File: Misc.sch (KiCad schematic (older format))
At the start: 22 parts, among them U3 PCF8523TK, U4 TLV70218DBV, U5 CDCE913PW, U7 LM75BDP, U8 LM75BDP, X1 32768, X2 20MHz

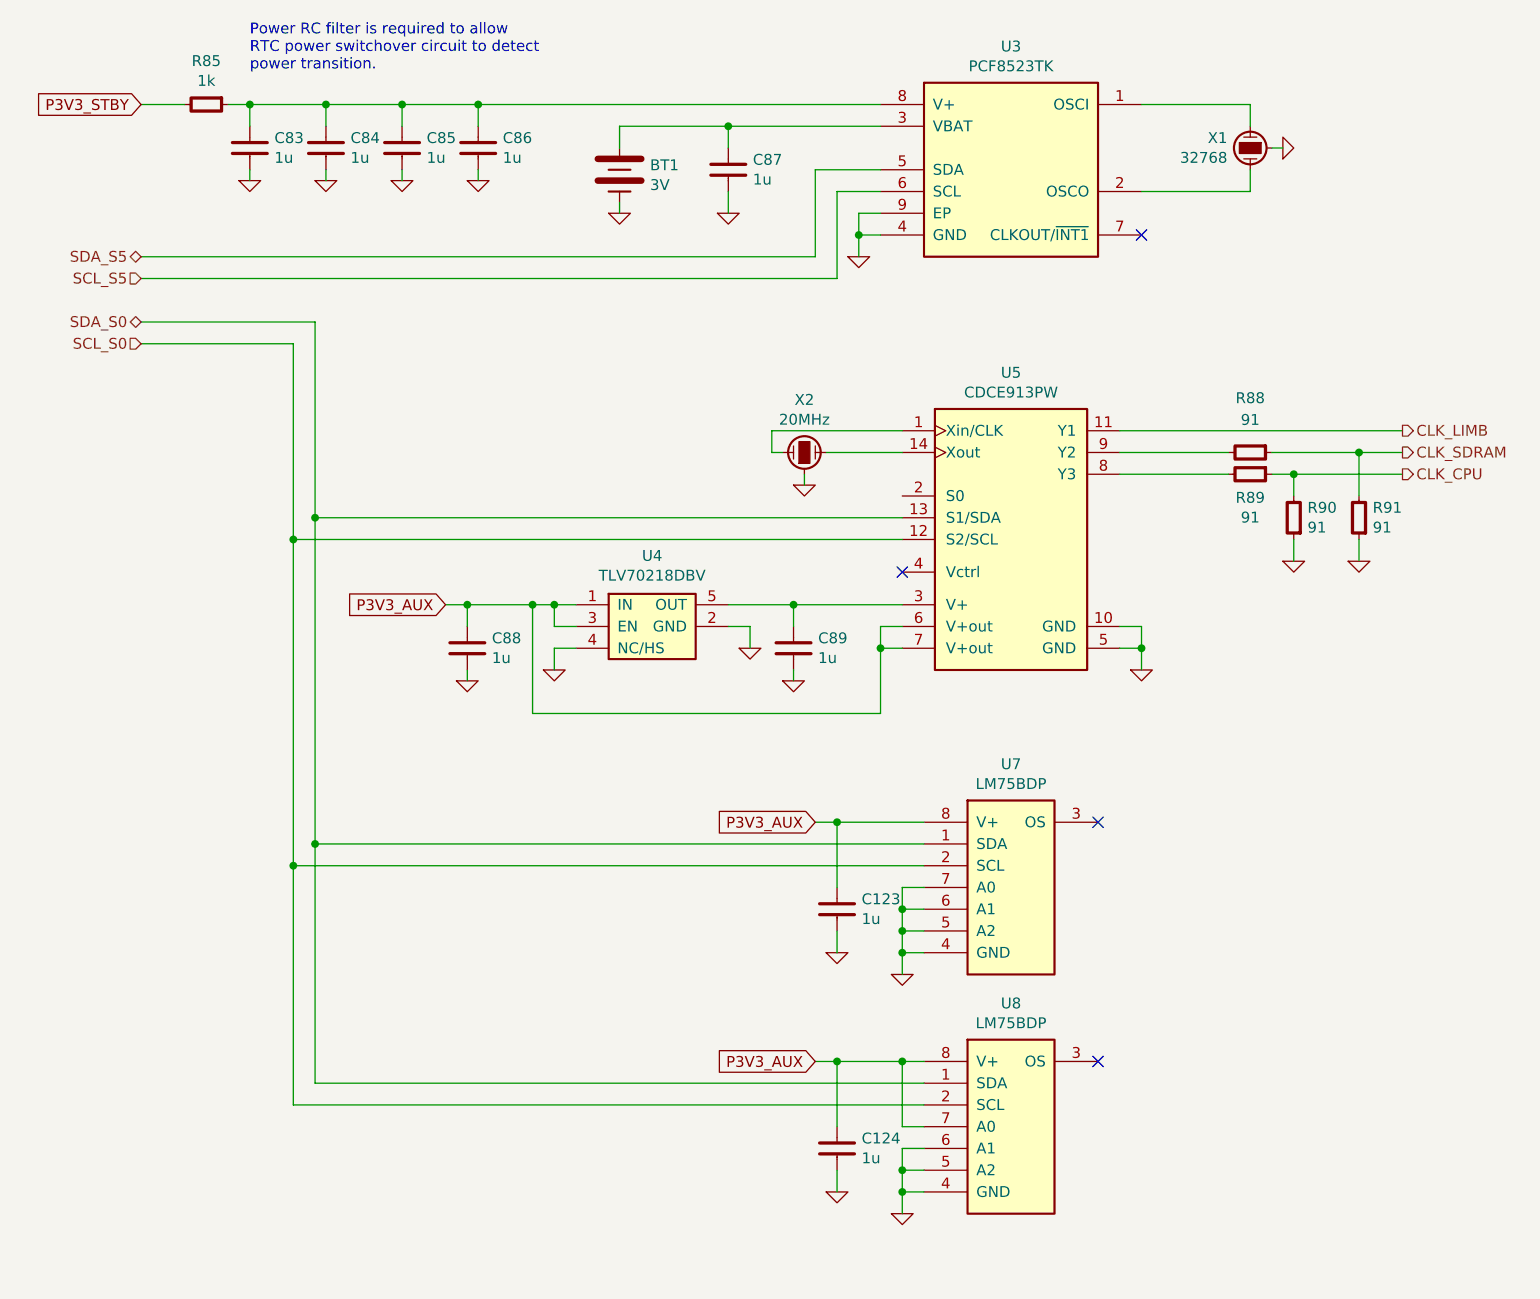
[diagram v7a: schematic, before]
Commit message: Tidy up Misc sheet
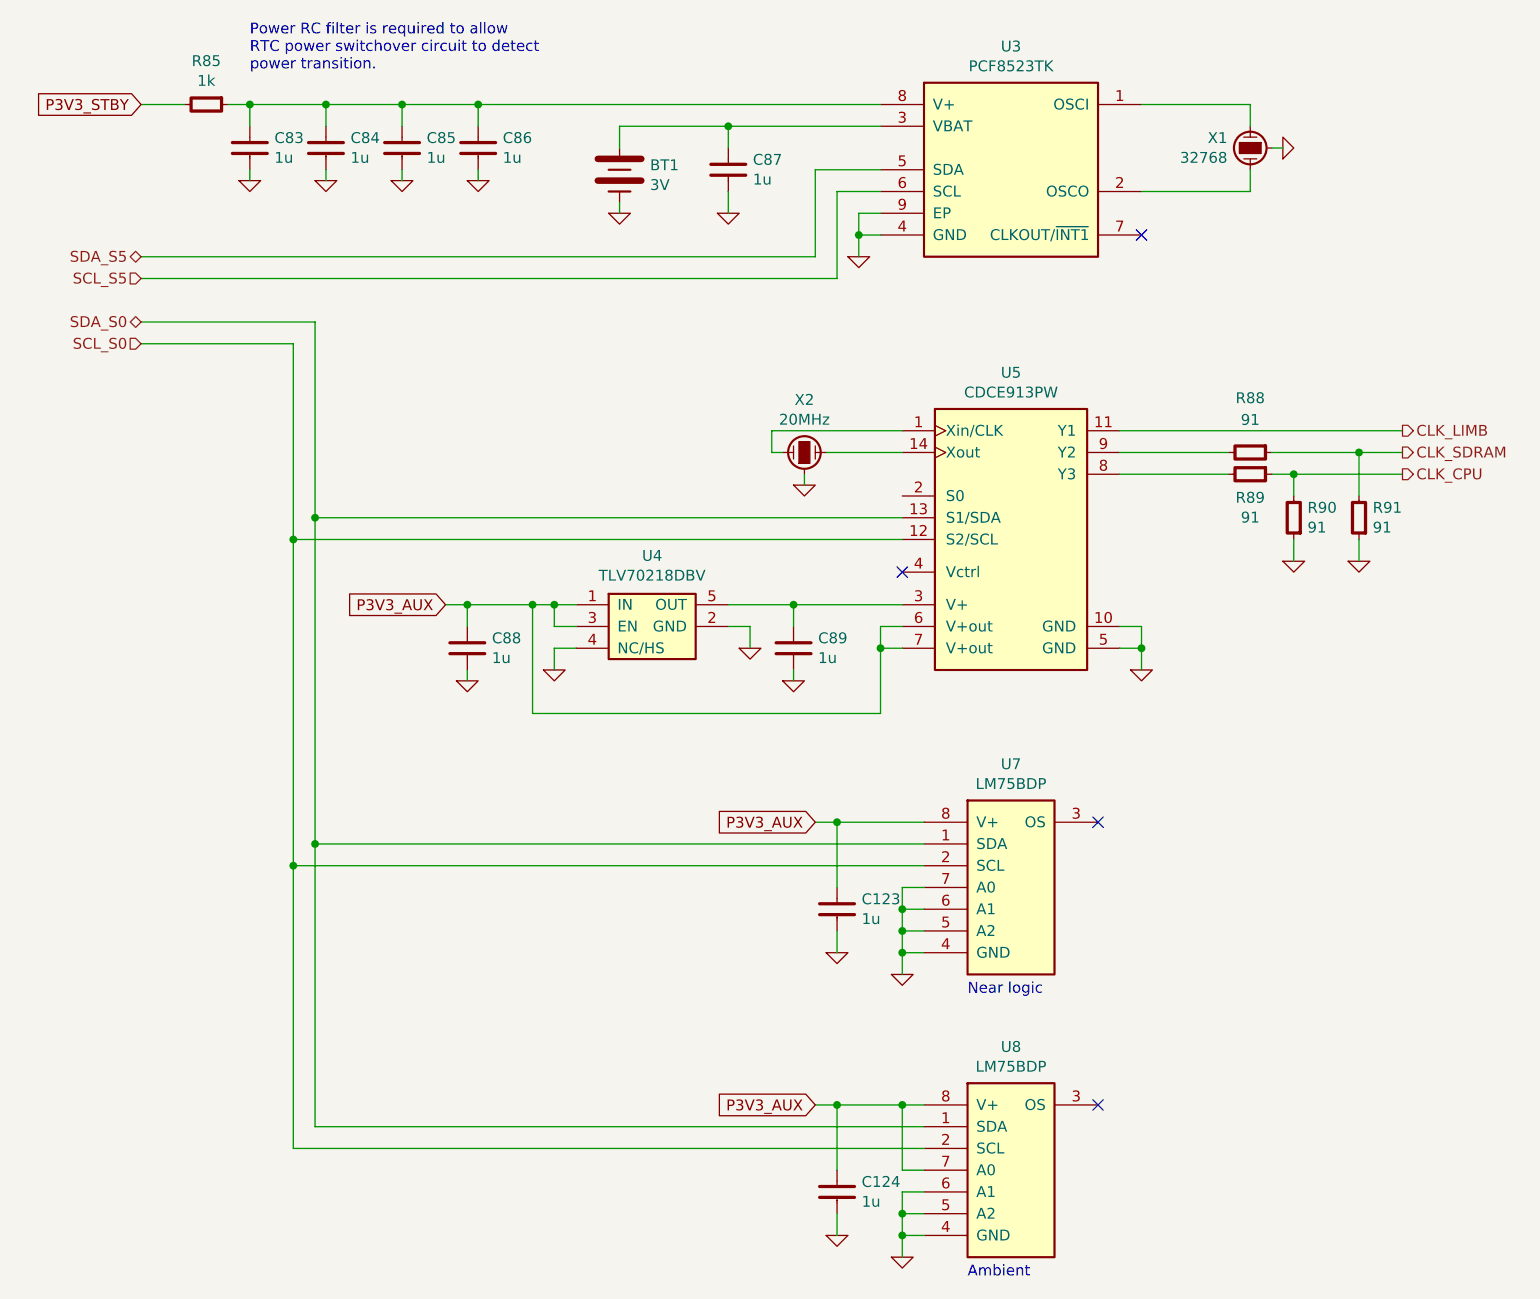
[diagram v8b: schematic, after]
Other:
- note added: "Ambient"
- note added: "Near logic"
- moved on the sheet: C124, U8
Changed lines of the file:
@@
 EELAYER 25 0
 EELAYER END
-$Descr A4 11693 8268
+$Descr A 11000 8500
 encoding utf-8
-Sheet 9 10
-Title ""
-Date ""
+Sheet 8 10
+Title "Miscellaneous peripherals"
+Date "2016-08-05"
 Rev ""
 Comp ""
@@
 	5000 2000 4900 2000
 Wire Wire Line
-	4900 2000 4900 2200
+	4900 2000 4900 2100
+Wire Wire Line
+	4900 2100 4900 2200
 Wire Wire Line
 	5000 2100 4900 2100
@@
 $EndComp
 Wire Wire Line
-	2000 1500 5000 1500
+	2000 1500 2100 1500
+Wire Wire Line
+	2100 1500 2450 1500
+Wire Wire Line
+	2450 1500 2800 1500
+Wire Wire Line
+	2800 1500 3150 1500
+Wire Wire Line
+	3150 1500 5000 1500
 $Comp
 L C-0402 C?
@@
 $EndComp
 Wire Wire Line
-	3800 1600 5000 1600
+	3800 1600 4300 1600
+Wire Wire Line
+	4300 1600 5000 1600
 Wire Wire Line
 	3800 1600 3800 1700
@@
 	6100 3900 6200 3900
 Wire Wire Line
-	6200 3900 6200 4100
+	6200 3900 6200 4000
+Wire Wire Line
+	6200 4000 6200 4100
 Wire Wire Line
 	6200 4000 6100 4000
@@
 $EndComp
 Wire Wire Line
-	4300 3800 5100 3800
+	4300 3800 4600 3800
+Wire Wire Line
+	4600 3800 5100 3800
 $Comp
 L GND #PWR161
@@
 	3500 3900 3500 3800
 Wire Wire Line
-	3000 3800 3600 3800
+	3000 3800 3100 3800
+Wire Wire Line
+	3100 3800 3400 3800
+Wire Wire Line
+	3400 3800 3500 3800
+Wire Wire Line
+	3500 3800 3600 3800
 Connection ~ 3500 3800
 Text GLabel 3000 3800 0    50   Input ~ 0
@@
 	4600 4150 4600 4100
 Wire Wire Line
-	5000 4300 5000 3900
+	5000 4300 5000 4000
+Wire Wire Line
+	5000 4000 5000 3900
 $Comp
 L LM75BDP U7
@@
 P3V3_AUX
 Wire Wire Line
-	4700 4800 5200 4800
+	4700 4800 4800 4800
+Wire Wire Line
+	4800 4800 5200 4800
 Text HLabel 1600 2500 0    50   BiDi ~ 0
 SDA_S0
@@
 	1600 2500 2400 2500
 Wire Wire Line
-	2400 2500 2400 6000
-Wire Wire Line
-	2300 2600 2300 6100
+	2400 2500 2400 3400
+Wire Wire Line
+	2400 3400 2400 4900
+Wire Wire Line
+	2400 4900 2400 6200
+Wire Wire Line
+	2300 2600 2300 3500
+Wire Wire Line
+	2300 3500 2300 5000
+Wire Wire Line
+	2300 5000 2300 6300
 Wire Wire Line
 	2300 2600 1600 2600
@@
 $EndComp
 Wire Wire Line
-	5100 5100 5100 5500
+	5100 5100 5100 5200
+Wire Wire Line
+	5100 5200 5100 5300
+Wire Wire Line
+	5100 5300 5100 5400
+Wire Wire Line
+	5100 5400 5100 5500
 Wire Wire Line
 	5100 5100 5200 5100
@@
 L LM75BDP U8
 U 1 1 579F50E6
-P 5600 5900
-F 0 "U8" H 5600 6167 50  0000 C CNN
-F 1 "LM75BDP" H 5600 6076 50  0000 C CNN
-F 2 "IPC7351-Nominal:SOP65P490X110-8" H 5600 5100 50  0001 C CNN
-F 3 "http://www.nxp.com/documents/data_sheet/LM75B.pdf" H 5600 4900 50  0001 C CNN
-F 4 "IC NXP LM75BDP" H 5600 5000 50  0001 C CNN "BOM"
-	1    5600 5900
-	1    0    0    -1
-$EndComp
-NoConn ~ 6000 5900
-Text GLabel 4700 5900 0    50   Input ~ 0
+P 5600 6100
+F 0 "U8" H 5600 6367 50  0000 C CNN
+F 1 "LM75BDP" H 5600 6276 50  0000 C CNN
+F 2 "IPC7351-Nominal:SOP65P490X110-8" H 5600 5300 50  0001 C CNN
+F 3 "http://www.nxp.com/documents/data_sheet/LM75B.pdf" H 5600 5100 50  0001 C CNN
+F 4 "IC NXP LM75BDP" H 5600 5200 50  0001 C CNN "BOM"
+	1    5600 6100
+	1    0    0    -1
+$EndComp
+NoConn ~ 6000 6100
+Text GLabel 4700 6100 0    50   Input ~ 0
 P3V3_AUX
 Wire Wire Line
-	4700 5900 5200 5900
-Wire Wire Line
-	2400 6000 5200 6000
+	4700 6100 4800 6100
+Wire Wire Line
+	4800 6100 5100 6100
+Wire Wire Line
+	5100 6100 5200 6100
+Wire Wire Line
+	2400 6200 5200 6200
 Connection ~ 2400 4900
 Wire Wire Line
-	2300 6100 5200 6100
+	2300 6300 5200 6300
 Connection ~ 2300 5000
 Wire Wire Line
-	5200 6300 5100 6300
-Wire Wire Line
-	5100 6300 5100 6600
+	5200 6500 5100 6500
+Wire Wire Line
+	5100 6500 5100 6600
+Wire Wire Line
+	5100 6600 5100 6700
+Wire Wire Line
+	5100 6700 5100 6800
 $Comp
 L GND #PWR168
 U 1 1 579F532E
-P 5100 6600
-F 0 "#PWR168" H 5100 6600 30  0001 C CNN
-F 1 "GND" H 5100 6530 30  0001 C CNN
-F 2 "" H 5100 6600 60  0000 C CNN
-F 3 "" H 5100 6600 60  0000 C CNN
-	1    5100 6600
-	1    0    0    -1
-$EndComp
+P 5100 6800
+F 0 "#PWR168" H 5100 6800 30  0001 C CNN
+F 1 "GND" H 5100 6730 30  0001 C CNN
+F 2 "" H 5100 6800 60  0000 C CNN
+F 3 "" H 5100 6800 60  0000 C CNN
+	1    5100 6800
+	1    0    0    -1
+$EndComp
+Wire Wire Line
+	5200 6600 5100 6600
+Connection ~ 5100 6600
+Wire Wire Line
+	5200 6700 5100 6700
+Connection ~ 5100 6700
 Wire Wire Line
 	5200 6400 5100 6400
-Connection ~ 5100 6400
-Wire Wire Line
-	5200 6500 5100 6500
-Connection ~ 5100 6500
-Wire Wire Line
-	5200 6200 5100 6200
-Wire Wire Line
-	5100 6200 5100 5900
-Connection ~ 5100 5900
+Wire Wire Line
+	5100 6400 5100 6100
+Connection ~ 5100 6100
 $Comp
 L C-0402 C?
@@
 L C-0402 C?
 U 1 1 579F605F
-P 4800 6300
+P 4800 6500
 AR Path="/5765A5BA/579F605F" Ref="C?"  Part="1"
 AR Path="/5765B2E6/579F605F" Ref="C?"  Part="1"
 AR Path="/57981212/579F605F" Ref="C124"  Part="1"
-F 0 "C124" H 4913 6346 50  0000 L CNN
-F 1 "1u" H 4913 6255 50  0000 L CNN
-F 2 "IPC7351-Nominal:CAPC1005X55" H 4800 6300 50  0001 C CNN
-F 3 "http://psearch.en.murata.com/capacitor/product/GRM155C80J105KE15%23.html" H 4790 6275 60  0001 C CNN
-F 4 "DIST DIGIKEY 490-6281-1-ND" H 5600 6850 60  0001 C CNN "BOM"
-	1    4800 6300
-	1    0    0    -1
-$EndComp
-Wire Wire Line
-	4800 6200 4800 5900
-Connection ~ 4800 5900
+F 0 "C124" H 4913 6546 50  0000 L CNN
+F 1 "1u" H 4913 6455 50  0000 L CNN
+F 2 "IPC7351-Nominal:CAPC1005X55" H 4800 6500 50  0001 C CNN
+F 3 "http://psearch.en.murata.com/capacitor/product/GRM155C80J105KE15%23.html" H 4790 6475 60  0001 C CNN
+F 4 "DIST DIGIKEY 490-6281-1-ND" H 5600 7050 60  0001 C CNN "BOM"
+	1    4800 6500
+	1    0    0    -1
+$EndComp
+Wire Wire Line
+	4800 6400 4800 6100
+Connection ~ 4800 6100
 $Comp
 L GND #PWR165
 U 1 1 579F6133
-P 4800 6500
-F 0 "#PWR165" H 4800 6500 30  0001 C CNN
-F 1 "GND" H 4800 6430 30  0001 C CNN
-F 2 "" H 4800 6500 60  0000 C CNN
-F 3 "" H 4800 6500 60  0000 C CNN
-	1    4800 6500
-	1    0    0    -1
-$EndComp
-Wire Wire Line
-	4800 6500 4800 6400
+P 4800 6700
+F 0 "#PWR165" H 4800 6700 30  0001 C CNN
+F 1 "GND" H 4800 6630 30  0001 C CNN
+F 2 "" H 4800 6700 60  0000 C CNN
+F 3 "" H 4800 6700 60  0000 C CNN
+	1    4800 6700
+	1    0    0    -1
+$EndComp
+Wire Wire Line
+	4800 6700 4800 6600
 Wire Wire Line
 	6100 3000 7400 3000
@@
 	6600 3100 6100 3100
 Wire Wire Line
-	6800 3100 7400 3100
+	6800 3100 7200 3100
+Wire Wire Line
+	7200 3100 7400 3100
 $Comp
 L R-0402 R89
@@
 $EndComp
 Wire Wire Line
-	6800 3200 7400 3200
+	6800 3200 6900 3200
+Wire Wire Line
+	6900 3200 7400 3200
 Wire Wire Line
 	6600 3200 6100 3200
@@
 Wire Wire Line
 	4650 3250 4650 3200
+Text Notes 5400 6900 0    50   ~ 0
+Ambient
+Text Notes 5400 5600 0    50   ~ 0
+Near logic
 $EndSCHEMATC
